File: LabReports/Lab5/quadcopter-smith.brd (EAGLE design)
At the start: 60 x 60 mm, 58 parts, among them J1 AVR_SPI_PRG_6NS, Q1 SI2302CDS, Q2 SI2302CDS, Q3 SI2302CDS, Q4 SI2302CDS, U1 ATMEGA128RFA1, U2 LSM9DS0-LGA24, Y1 16MHz

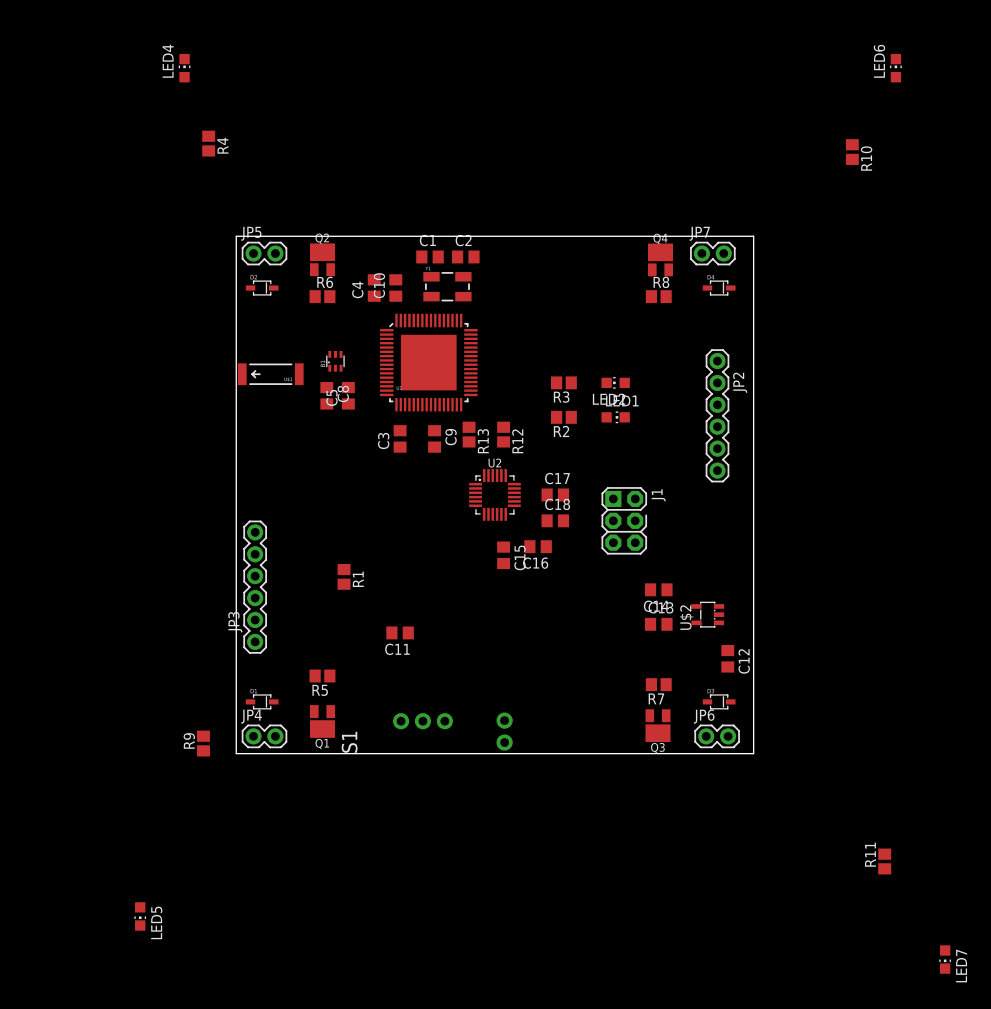
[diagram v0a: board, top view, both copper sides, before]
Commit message: board outline mockup, time to try routing!
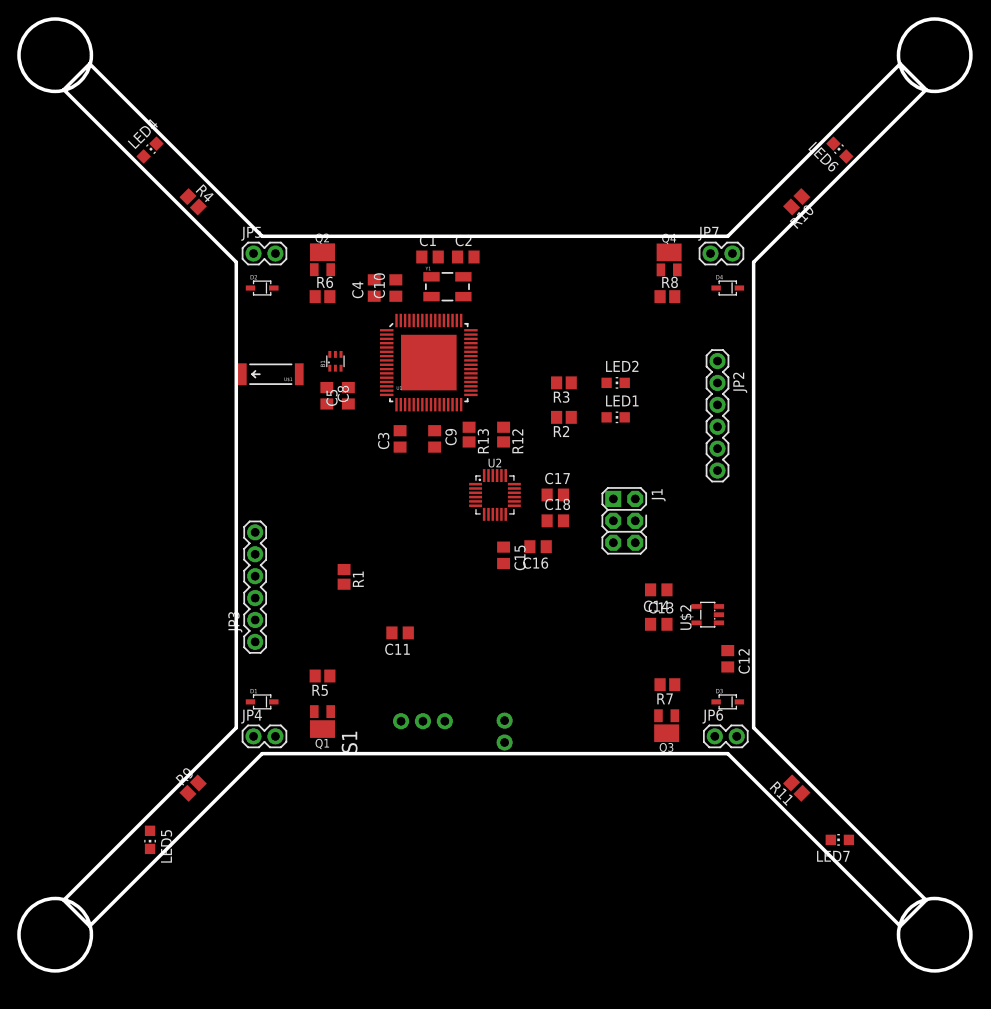
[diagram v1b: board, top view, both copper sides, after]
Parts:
- moved LED7 18.5 mm to (40.0, -40.0), turned to 90 degrees
- moved R11 13.3 mm to (35.0, -34.0), turned to 135 degrees
- moved LED6 11.5 mm to (40.0, 40.0), turned to 45 degrees
- moved LED4 10.3 mm to (-40.0, 40.0), turned to 315 degrees
- moved LED5 8.95 mm to (-40.0, -40.0)
- moved R10 8.65 mm to (35.0, 34.0), turned to 225 degrees
- moved R4 6.99 mm to (-35.0, 34.0), turned to 315 degrees
- moved R9 5.31 mm to (-35.0, -34.0), turned to 45 degrees
- moved D3 1.00 mm to (27.0, -24.0)
- moved D4 1.00 mm to (27.0, 24.0)
- moved JP6 1.00 mm to (25.5, -28.0)
- moved JP7 1.00 mm to (25.0, 28.0)
- moved Q3 1.00 mm to (19.9, -26.5)
- moved Q4 1.00 mm to (20.2, 27.0)
- moved R7 1.00 mm to (20.0, -22.0)
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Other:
- board size 60 x 60 mm -> 110.4 x 110.4 mm

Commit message: end of Thursday lab hours
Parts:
- moved D2 3.00 mm to (-24.0, 24.0)
- moved JP1 3.00 mm to (4.12, -26.2)
- moved D1 2.00 mm to (-25.0, -24.0)
- moved D3 2.00 mm to (25.0, -24.0)
- moved D4 2.00 mm to (25.0, 24.0)
- moved JP4 2.00 mm to (-26.0, -28.0)
- moved JP5 2.00 mm to (-26.0, 28.0)
- moved JP6 2.00 mm to (23.5, -28.0)
- moved Q1 2.00 mm to (-18.0, -26.0)
- moved Q3 2.00 mm to (17.9, -26.5)
- moved Q4 2.00 mm to (18.2, 27.0)
- moved R5 2.00 mm to (-18.0, -21.0)
- moved R7 2.00 mm to (18.0, -22.0)
- moved R8 2.00 mm to (18.0, 23.0)
- moved S1 2.00 mm to (-6.35, -26.2)
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
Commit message: shrink, route, modified some parts in Lab5.lbr
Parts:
- moved C11 38.6 mm to (15.0, 12.5)
- moved C10 23.9 mm to (7.50, 9.50)
- moved JP1 14.2 mm to (5.00, -12.0)
- moved C1 13.9 mm to (2.00, 17.5), turned to 90 degrees
- moved JP4 12.8 mm to (-19.0, -17.2), turned to 315 degrees
- moved C4 12.6 mm to (-6.00, 14.2), turned to 180 degrees
- moved JP5 12.6 mm to (-17.2, 19.0), turned to 225 degrees
- moved D1 12.0 mm to (-16.0, -16.0), turned to 315 degrees
- moved D3 12.0 mm to (16.0, -16.0), turned to 45 degrees
- moved D4 12.0 mm to (16.0, 16.0), turned to 315 degrees
- moved R1 11.8 mm to (-8.00, -2.50)
- moved Q2 11.7 mm to (-11.5, 18.0)
- moved U$1 11.7 mm to (-17.2, 6.25)
- moved B1 11.3 mm to (-11.0, 7.00)
- moved C5 11.3 mm to (-9.50, 3.00), turned to 270 degrees
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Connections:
- net GND: no longer U1.65
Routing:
- net 3V: track 0.00 -> 61.2 mm
- net VBAT: track 0.00 -> 47.2 mm
- net GND: track 0.00 -> 19.2 mm, vias 0 -> 12
- net RX0: track 0.00 -> 18.0 mm
- net TX0: track 0.00 -> 17.2 mm
- net MOSI: track 0.00 -> 14.3 mm
- net SCK: track 0.00 -> 11.5 mm
- net MISO: track 0.00 -> 10.9 mm
- net N$2: track 0.00 -> 10.6 mm
- net N$20: track 0.00 -> 8.86 mm
- net N$11: track 0.00 -> 8.86 mm
- net SDA: track 0.00 -> 8.85 mm, vias 0 -> 2
- net SCL: track 0.00 -> 8.44 mm
- net RESET: track 0.00 -> 8.23 mm
- net PB6: track 0.00 -> 7.70 mm
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- added copper zone on layer 1, net GND
- added copper zone on layer 16, net GND
- added copper zone on layer 1, net N$9
- added copper zone on layer 1, net VBAT
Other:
- board size 110.4 x 110.4 mm -> 95.4 x 95.4 mm

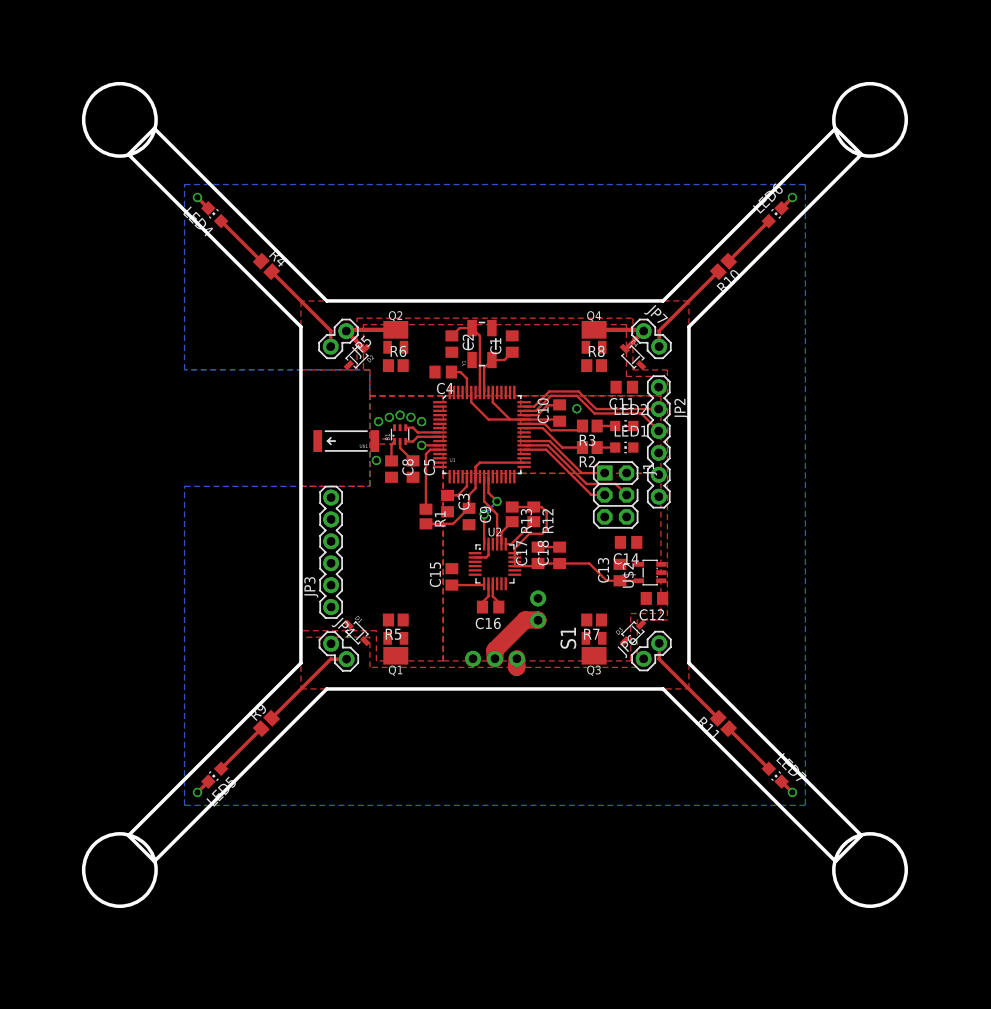
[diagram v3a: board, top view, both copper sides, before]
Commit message: Binged on manual routing
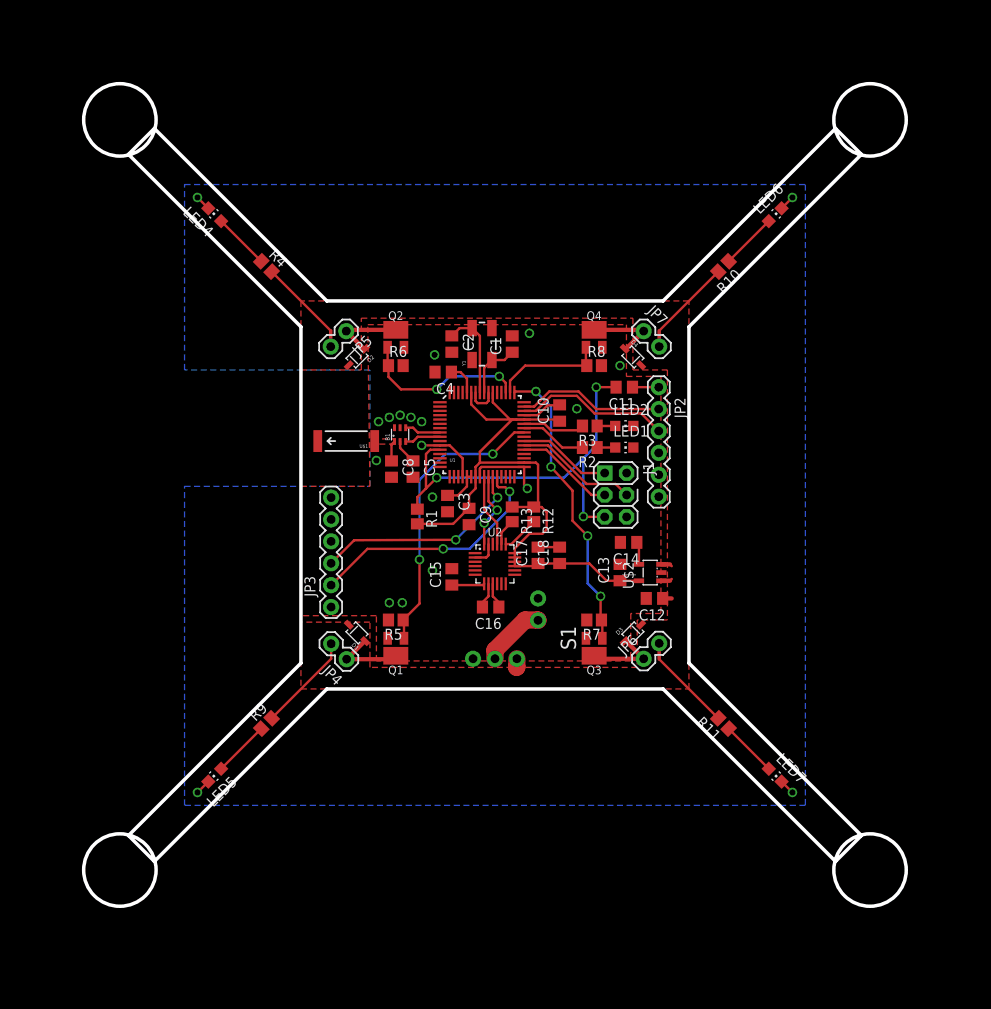
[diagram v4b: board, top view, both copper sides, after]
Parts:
- R12, R13: value (none) -> 10k
- moved JP4 2.55 mm to (-17.2, -19.1), turned to 135 degrees
- moved R1 1.00 mm to (-9.00, -2.50)
- turned D1 to 135 degrees
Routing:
- net RESET: track 8.23 -> 48.8 mm, vias 0 -> 3
- net PE3: track 0.00 -> 34.3 mm, vias 0 -> 4
- net PB5: track 0.00 -> 33.6 mm, vias 0 -> 2
- net TX1: track 0.00 -> 29.2 mm, vias 0 -> 2
- net RX1: track 0.00 -> 25.1 mm, vias 0 -> 2
- net PE5: track 0.00 -> 19.7 mm, vias 0 -> 2
- net GND: track 19.2 -> 37.1 mm, vias 12 -> 20
- net 3V: track 61.2 -> 76.0 mm
- net PE4: track 0.00 -> 13.2 mm
- net N$19: track 0.00 -> 8.95 mm
- net N$18: track 0.00 -> 8.89 mm
- net VBAT: track 47.2 -> 50.7 mm
- net N$15: track 0.00 -> 3.05 mm
- net N$16: track 0.00 -> 2.65 mm
- net N$3: track 3.80 -> 4.30 mm
